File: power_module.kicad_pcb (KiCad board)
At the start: 4 copper layers, 95 x 110 mm, 71 parts, among them J1 USB_C_PD, J2 OUTPUT, J3 I2C_BREAKOUT, Q1 DUAL_N_FET, Q2 DUAL_N_FET, Q3 DUAL_N_FET, Q4 DUAL_N_FET, SW1 ON_OFF, U1 BQ7692003, U2 CH224K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

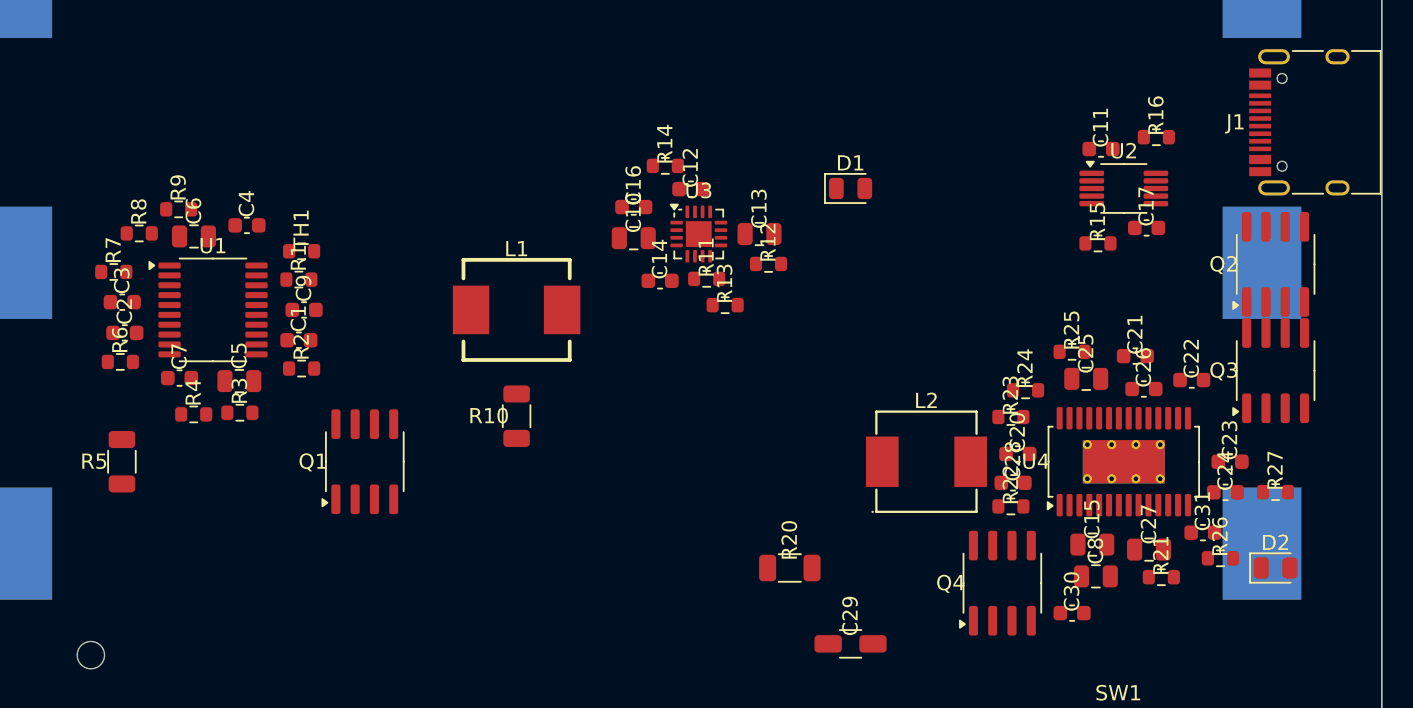
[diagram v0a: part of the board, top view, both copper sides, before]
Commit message: pcb: post-user spread pass — relieve crowding around U1 and U4
User adjustment pass moved BAT1 up and components into a compact
lower band; cluster-density check showed 17 components within 8mm
of U1 (BMS) and 17 within 8mm of U4 (buck-boost), too tight to route.

This pass:
  - Shifts U4 +6mm right (84,88) for thermal/edge clearance from
    BAT1 cell holder B.Cu pads (user-suggested in case the integrity-
    checker NPTH-via false positive was actually a ventilation concern).
  - Re-places 39 small parts via pin-targeted place_near against the
    correct U1 / U3 / U4 pad numbers, honoring the C9 → U1.9 explicit
    Placement_Anchor (the one the user noticed had missed last pass).
  - Fixes a Q2/Q3 mis-assumption: Q2 is actually the BQ24650 charger
    sync FET (BQ_HIDRV/BQ_LODRV/BQ_PH), not a buck-boost FET. Moved
    Q2 to the charger area near U3.14, Q3 stays near U4.28 as the
    BB_SW1-leg buck-boost FET.
  - Moves R27 out of U4's footprint into the D2 LED cluster.

0 integrity findings (no pad overlaps, no courtyard overlaps).
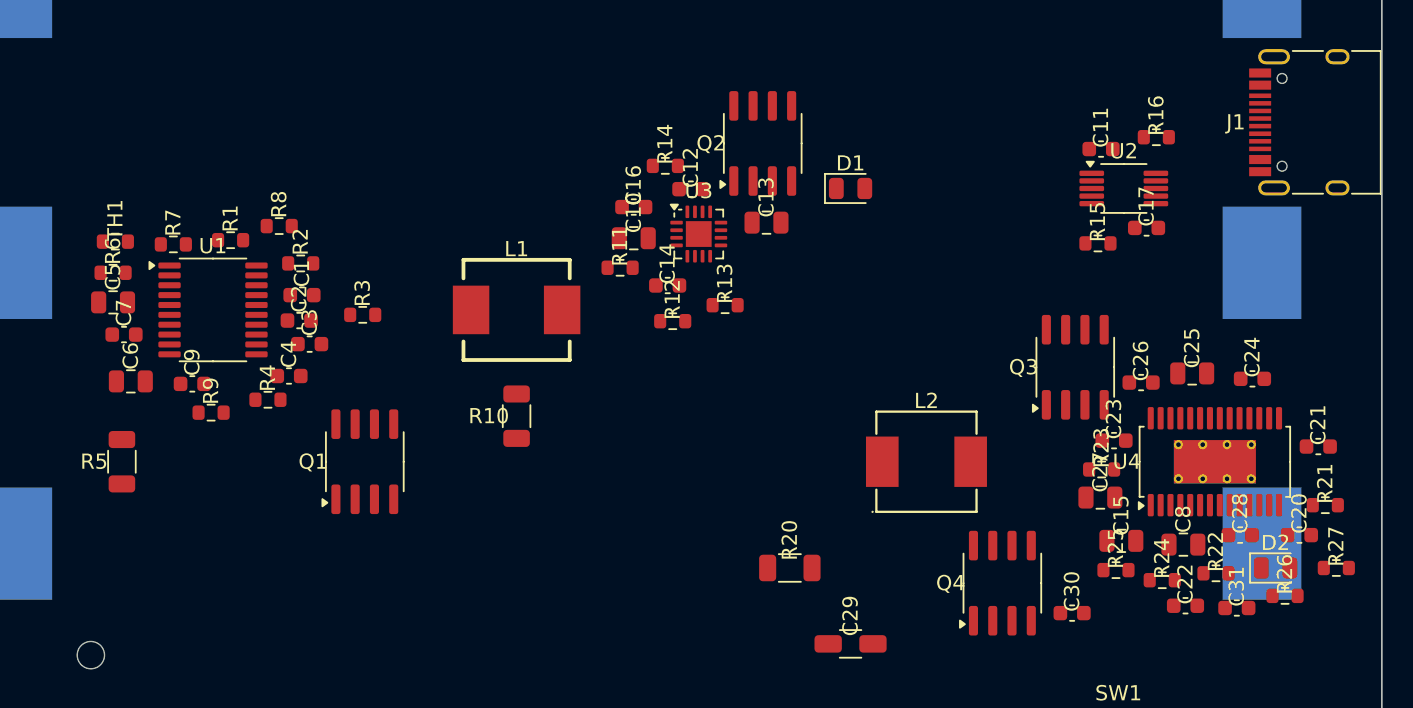
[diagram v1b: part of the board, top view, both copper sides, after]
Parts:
- moved Q2 34.7 mm to (54.2, 67.0)
- moved C20 19.3 mm to (89.6, 92.8)
- moved R24 15.4 mm to (80.5, 95.8)
- moved C28 15.4 mm to (85.7, 92.8)
- moved C22 14.9 mm to (82.1, 97.5)
- moved R25 14.7 mm to (77.5, 95.1)
- moved R22 14.2 mm to (84.1, 95.4)
- moved R9 13.6 mm to (17.9, 84.8)
- moved C21 13.4 mm to (90.8, 87.0)
- moved Q3 13.2 mm to (74.8, 81.8)
- moved C3 12.7 mm to (24.4, 80.3)
- moved TH1 12.3 mm to (11.6, 73.5)
- moved R21 11.8 mm to (91.3, 90.9)
- moved C2 11.5 mm to (23.7, 78.7)
- moved C6 10.4 mm to (12.6, 82.7)
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
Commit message: More minor shifting
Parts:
- moved SW1 33.2 mm to (91.5, 76.3), turned to 90 degrees
- moved C21 10.4 mm to (92.1, 97.3)
- moved R21 8.85 mm to (88.8, 99.4)
- moved U4 4.33 mm to (88.3, 87.8)
- moved C25 4.07 mm to (86.5, 81.7)
- moved C24 3.51 mm to (89.9, 81.8)
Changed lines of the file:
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@@
 	(footprint "Button_Switch_SMD:SW_SPDT_PCM12"
 		(layer "F.Cu")
-		(at 77.652724 106.455135)
+		(at 91.459276 76.250559 90)
 		(descr "Ultraminiature Surface Mount Slide Switch, right-angle, https://www.ckswitches.com/media/1424/pcm.pdf")
 		(property "Reference" "SW1"
-			(at 0 -3.2 0)
+			(at 0 -3.2 90)
 			(layer "F.SilkS")
 			(effects
@@
 		)
 		(property "Value" "ON_OFF"
-			(at 0 4.25 0)
+			(at 0 4.25 90)
 			(layer "F.Fab")
 			(effects
@@
 		)
 		(property "Datasheet" ""
-			(at 0 0 0)
+			(at 0 0 90)
 			(unlocked yes)
 			(layer "F.Fab")
@@
 		)
 		(property "Description" ""
-			(at 0 0 0)
+			(at 0 0 90)
 			(unlocked yes)
 			(layer "F.Fab")
@@
 		(attr smd)
 		(fp_line
-			(start -3.45 -0.07)
-			(end -3.45 0.72)
+			(start 1.4 -1.12)
+			(end 1.6 -1.12)
 			(stroke
 				(width 0.12)
@@
 		)
 		(fp_line
-			(start -2.85 1.73)
-			(end 2.85 1.73)
+			(start -1.6 -1.12)
+			(end 0.1 -1.12)
 			(stroke
 				(width 0.12)
@@
 		)
 		(fp_line
-			(start -1.6 -1.12)
-			(end 0.1 -1.12)
+			(start -3.45 -0.07)
+			(end -3.45 0.719999)
 			(stroke
 				(width 0.12)
@@
 		)
 		(fp_line
-			(start -1.4 1.73)
-			(end -1.4 3.02)
+			(start 3.45 0.719999)
+			(end 3.45 -0.07)
 			(stroke
 				(width 0.12)
@@
 		)
 		(fp_line
-			(start -1.4 3.02)
-			(end -1.2 3.23)
+			(start -1.4 1.73)
+			(end -1.4 3.02)
 			(stroke
 				(width 0.12)
@@
 		)
 		(fp_line
-			(start -1.2 3.23)
-			(end -0.3 3.23)
+			(start -2.85 1.73)
+			(end 2.85 1.73)
 			(stroke
 				(width 0.12)
@@
 		(fp_line
 			(start -0.1 3.02)
-			(end -0.3 3.23)
+			(end -0.1 1.73)
 			(stroke
 				(width 0.12)
@@
 		(fp_line
 			(start -0.1 3.02)
-			(end -0.1 1.73)
+			(end -0.3 3.23)
 			(stroke
 				(width 0.12)
@@
 		)
 		(fp_line
-			(start 1.4 -1.12)
-			(end 1.6 -1.12)
+			(start -1.4 3.02)
+			(end -1.2 3.23)
 			(stroke
 				(width 0.12)
@@
 		)
 		(fp_line
-			(start 3.45 0.72)
-			(end 3.45 -0.07)
+			(start -1.2 3.23)
+			(end -0.3 3.23)
 			(stroke
 				(width 0.12)
@@
 		)
 		(fp_line
-			(start -4.4 -2.45)
-			(end 4.4 -2.45)
+			(start 4.4 -2.45)
+			(end 4.4 2.1)
 			(stroke
 				(width 0.05)
@@
 		)
 		(fp_line
-			(start -4.4 2.1)
-			(end -4.4 -2.45)
+			(start -4.4 -2.45)
+			(end 4.4 -2.45)
 			(stroke
 				(width 0.05)
@@
 		)
 		(fp_line
-			(start -1.65 2.1)
-			(end -4.4 2.1)
+			(start 4.4 2.1)
+			(end 1.65 2.1)
 			(stroke
 				(width 0.05)
@@
 		)
 		(fp_line
-			(start -1.65 3.4)
-			(end -1.65 2.1)
+			(start 1.65 2.1)
+			(end 1.65 3.4)
 			(stroke
 				(width 0.05)
@@
 		)
 		(fp_line
-			(start 1.65 2.1)
-			(end 1.65 3.4)
+			(start -1.65 2.1)
+			(end -4.4 2.1)
 			(stroke
 				(width 0.05)
@@
 		)
 		(fp_line
-			(start 1.65 3.4)
-			(end -1.65 3.4)
+			(start -4.4 2.1)
+			(end -4.4 -2.45)
 			(stroke
 				(width 0.05)
@@
 		)
 		(fp_line
-			(start 4.4 -2.45)
-			(end 4.4 2.1)
+			(start 1.65 3.4)
+			(end -1.65 3.4)
 			(stroke
 				(width 0.05)
@@
 		)
 		(fp_line
-			(start 4.4 2.1)
-			(end 1.65 2.1)
+			(start -1.65 3.4)
+			(end -1.65 2.1)
 			(stroke
 				(width 0.05)
@@
 		)
 		(fp_line
-			(start -3.35 -1)
-			(end -3.35 1.6)
+			(start 3.35 -1)
+			(end -3.35 -1)
 			(stroke
 				(width 0.1)
@@
 		)
 		(fp_line
-			(start -3.35 1.6)
-			(end 3.35 1.6)
+			(start -3.35 -1)
+			(end -3.35 1.6)
 			(stroke
 				(width 0.1)
@@
 		)
 		(fp_line
-			(start -1.4 1.65)
-			(end -1.4 2.95)
+			(start 3.35 1.6)
+			(end 3.35 -1)
 			(stroke
 				(width 0.1)
@@
 		)
 		(fp_line
-			(start -1.4 2.95)
-			(end -1.2 3.15)
+			(start -3.35 1.6)
+			(end 3.35 1.6)
 			(stroke
 				(width 0.1)
@@
 		)
 		(fp_line
-			(start -1.2 3.15)
-			(end -0.35 3.15)
+			(start -1.4 1.65)
+			(end -1.399999 2.95)
 			(stroke
 				(width 0.1)
@@
 		)
 		(fp_line
-			(start -0.35 3.15)
-			(end -0.15 2.95)
+			(start -0.1 2.9)
+			(end -0.1 1.6)
 			(stroke
 				(width 0.1)
@@
 		)
 		(fp_line
-			(start -0.1 2.9)
-			(end -0.1 1.6)
+			(start -1.399999 2.95)
+			(end -1.2 3.149999)
 			(stroke
 				(width 0.1)
@@
 		)
 		(fp_line
-			(start 3.35 -1)
-			(end -3.35 -1)
+			(start -1.2 3.149999)
+			(end -0.35 3.15)
 			(stroke
 				(width 0.1)
@@
 		)
 		(fp_line
-			(start 3.35 1.6)
-			(end 3.35 -1)
+			(start -0.35 3.15)
+			(end -0.15 2.95)
 			(stroke
 				(width 0.1)
@@
 		)
 		(fp_text user "${REFERENCE}"
-			(at 0 -3.2 0)
+			(at 0 -3.2 90)
 			(layer "F.Fab")
 			(effects
@@
 		)
 		(pad "" smd rect
-			(at -3.65 -0.78)
+			(at -3.65 -0.78 90)
 			(size 1 0.8)
 			(layers "F.Cu" "F.Mask" "F.Paste")
 		)
 		(pad "" smd rect
-			(at -3.65 1.43)
+			(at -3.65 1.43 90)
 			(size 1 0.8)
 			(layers "F.Cu" "F.Mask" "F.Paste")
 		)
 		(pad "" np_thru_hole circle
-			(at -1.5 0.33)
+			(at -1.5 0.33 90)
 			(size 0.9 0.9)
 			(drill 0.9)
@@
 		)
 		(pad "" np_thru_hole circle
-			(at 1.5 0.33)
+			(at 1.5 0.33 90)
 			(size 0.9 0.9)
 			(drill 0.9)
@@
 		)
 		(pad "" smd rect
-			(at 3.65 -0.78)
+			(at 3.65 -0.78 90)
 			(size 1 0.8)
 			(layers "F.Cu" "F.Mask" "F.Paste")
 		)
 		(pad "" smd rect
-			(at 3.65 1.43)
+			(at 3.65 1.43 90)
 			(size 1 0.8)
 			(layers "F.Cu" "F.Mask" "F.Paste")
 		)
 		(pad "1" smd rect
-			(at -2.25 -1.43)
+			(at -2.25 -1.43 90)
 			(size 0.7 1.5)
 			(layers "F.Cu" "F.Mask" "F.Paste")
@@
 		)
 		(pad "2" smd rect
-			(at 0.75 -1.43)
+			(at 0.75 -1.43 90)
 			(size 0.7 1.5)
 			(layers "F.Cu" "F.Mask" "F.Paste")
@@
 		)
 		(pad "3" smd rect
-			(at 2.25 -1.43)
+			(at 2.25 -1.43 90)
 			(size 0.7 1.5)
 			(layers "F.Cu" "F.Mask" "F.Paste")
@@
 	(footprint "Capacitor_SMD:C_0805_2012Metric"
 		(layer "F.Cu")
-		(at 82.504056 82.183077)
+		(at 86.541974 81.671148)
 		(descr "Capacitor SMD 0805 (2012 Metric), square (rectangular) end terminal, IPC-7351 nominal, (Body size source: IPC-SM-782 page 76, https://www.pcb-3d.com/wordpress/wp-content/uploads/ipc-sm-782a_amendment_1_and_2.pdf, https://docs.google.com/spreadsheets/d/1BsfQQcO9C6DZCsRaXUlFlo91Tg2WpOkGARC1WS5S8t0/edit?usp=sharing), generated with kicad-footprint-generator")
 		(tags "capacitor")
@@
 	(footprint "Resistor_SMD:R_0603_1608Metric"
 		(layer "F.Cu")
-		(at 91.275 90.8625)
+		(at 88.827926 99.365086)
 		(descr "Resistor SMD 0603 (1608 Metric), square (rectangular) end terminal, IPC-7351 nominal, (Body size source: IPC-SM-782 page 72, https://www.pcb-3d.com/wordpress/wp-content/uploads/ipc-sm-782a_amendment_1_and_2.pdf), generated with kicad-footprint-generator")
 		(tags "resistor")
@@
 	(footprint "Capacitor_SMD:C_0603_1608Metric"
 		(layer "F.Cu")
-		(at 90.812984 87.000126)
+		(at 92.149844 97.316627)
 		(descr "Capacitor SMD 0603 (1608 Metric), square (rectangular) end terminal, IPC-7351 nominal, (Body size source: IPC-SM-782 page 76, https://www.pcb-3d.com/wordpress/wp-content/uploads/ipc-sm-782a_amendment_1_and_2.pdf), generated with kicad-footprint-generator")
 		(tags "capacitor")
@@
 	(footprint "Capacitor_SMD:C_0603_1608Metric"
 		(layer "F.Cu")
-		(at 86.474999 82.539424)
+		(at 89.896687 81.760211)
 		(descr "Capacitor SMD 0603 (1608 Metric), square (rectangular) end terminal, IPC-7351 nominal, (Body size source: IPC-SM-782 page 76, https://www.pcb-3d.com/wordpress/wp-content/uploads/ipc-sm-782a_amendment_1_and_2.pdf), generated with kicad-footprint-generator")
 		(tags "capacitor")
@@
 	(footprint "Package_SO:HTSSOP-28-1EP_4.4x9.7mm_P0.65mm_EP2.85x5.4mm_ThermalVias"
 		(layer "F.Cu")
-		(at 84 88 90)
+		(at 88.327946 87.754013 90)
 		(descr "HTSSOP, 28 Pin (https://pdfserv.maximintegrated.com/package_dwgs/21-0108.PDF), generated with kicad-footprint-generator ipc_gullwing_generator.py")
 		(tags "HTSSOP SO")

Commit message: Inspecting progress
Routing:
- net V12_OUT: track 0.00 -> 52.8 mm
- net GND: vias 0 -> 33
- net BAT+: vias 0 -> 10

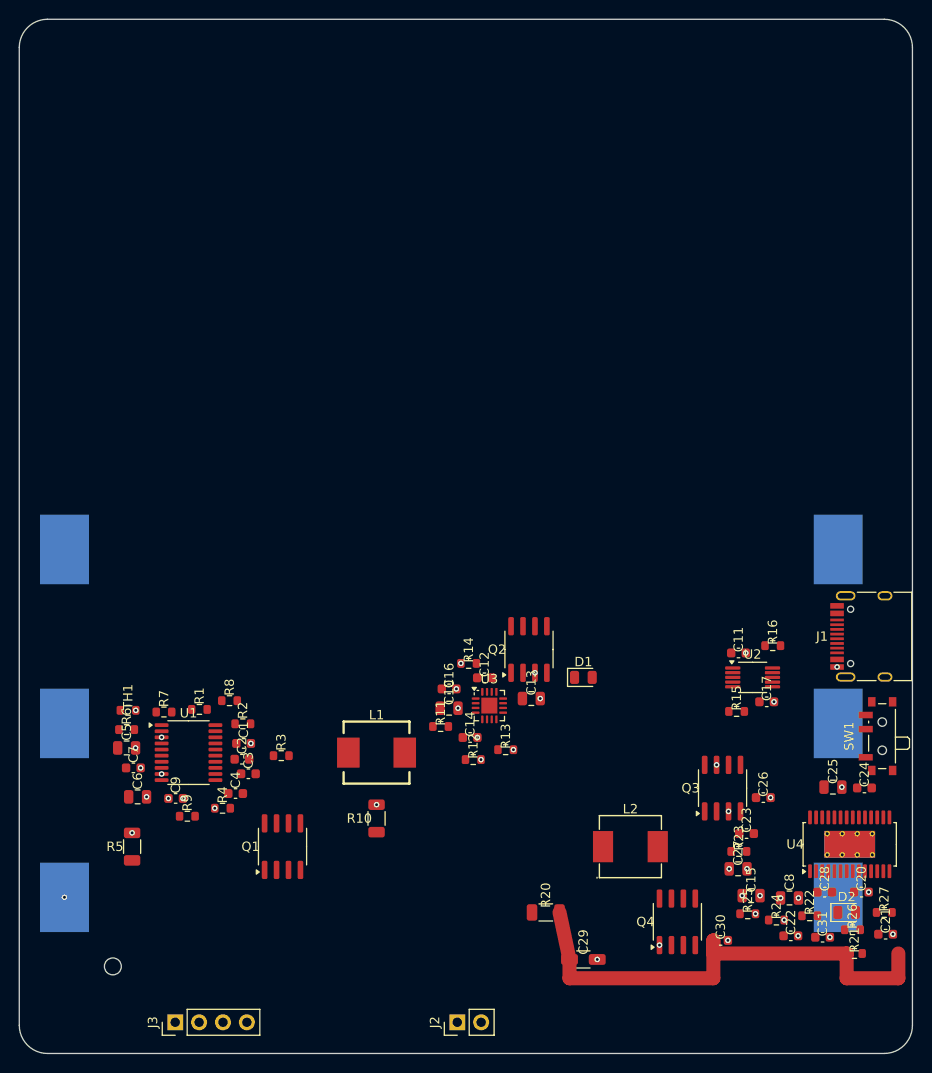
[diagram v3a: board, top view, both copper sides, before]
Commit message: pcb: north-spread BMS + charger into upper-half BAT1 envelope
Moved U1 BMS + Q1 + R5 sense + 17 satellites to NW quadrant (y=33-45),
moved U3 charger + L1 + R10 + Q2 + 9 satellites to NE quadrant
(y=35-45). Buck-boost U4 cluster stays south, output stage stays south.
The upper-half F.Cu was empty since BAT1 lives on B.Cu — used that
real estate to relieve density.

analyze_congestion result:
  - before: 5 cells score >= 238 (U1, U3, U4+BAT1, all ~270)
  - after: 2 cells score >= 238, both U4+BAT1 region (inherent
    buck-boost density). U1 and U3 hotspots dropped off the top-12.
  - active cells 85 -> 53, top score 272 -> 240.

Cell-sense routing also benefits: U1.VC pins are now at x=22-28 on
the left side of the board, ~17 mm from BAT1's left-side CELL pads
(x=4.8). Previously the path was ~85 mm round-trip.

0 errors / 1 warning (Q2/L1 minor courtyard overlap; nudged Q2).
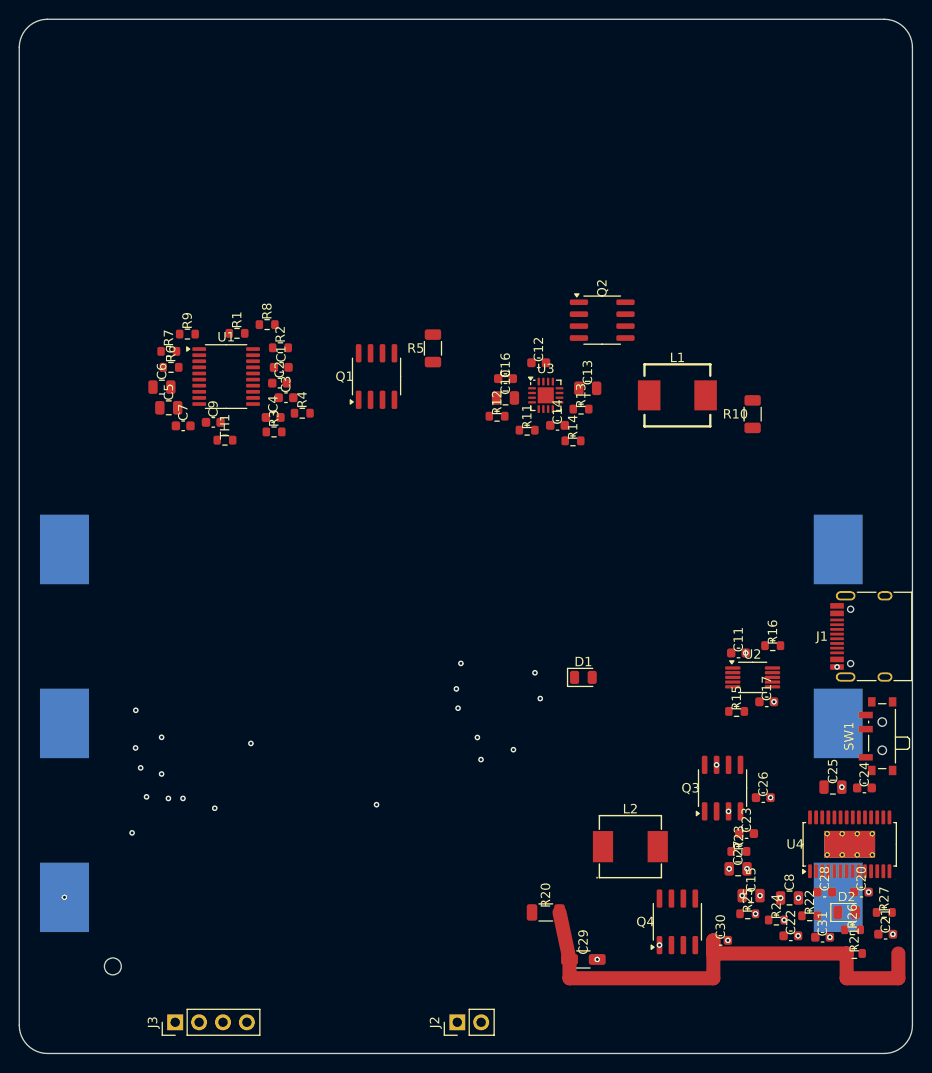
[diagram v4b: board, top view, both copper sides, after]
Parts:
- moved R5 61.9 mm to (44.0, 35.0)
- moved R10 58.7 mm to (78.0, 42.0)
- moved R9 51.3 mm to (17.9, 33.5)
- moved Q1 51.0 mm to (38.0, 38.0)
- moved L1 49.7 mm to (70.0, 40.0)
- moved C6 43.7 mm to (15.2, 39.1)
- moved R4 42.9 mm to (30.1, 41.9)
- moved C1 40.2 mm to (27.9, 37.0)
- moved C2 40.2 mm to (27.7, 38.7)
- moved C3 40.2 mm to (28.4, 40.3)
- moved C4 40.2 mm to (27.0, 42.4)
- moved C9 40.2 mm to (20.6, 42.9)
- moved R1 40.2 mm to (23.2, 33.4)
- moved R2 40.2 mm to (27.8, 34.9)
- moved R8 40.2 mm to (26.4, 32.5)
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
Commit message: Resized board and moved pieces back onto BAT1 area
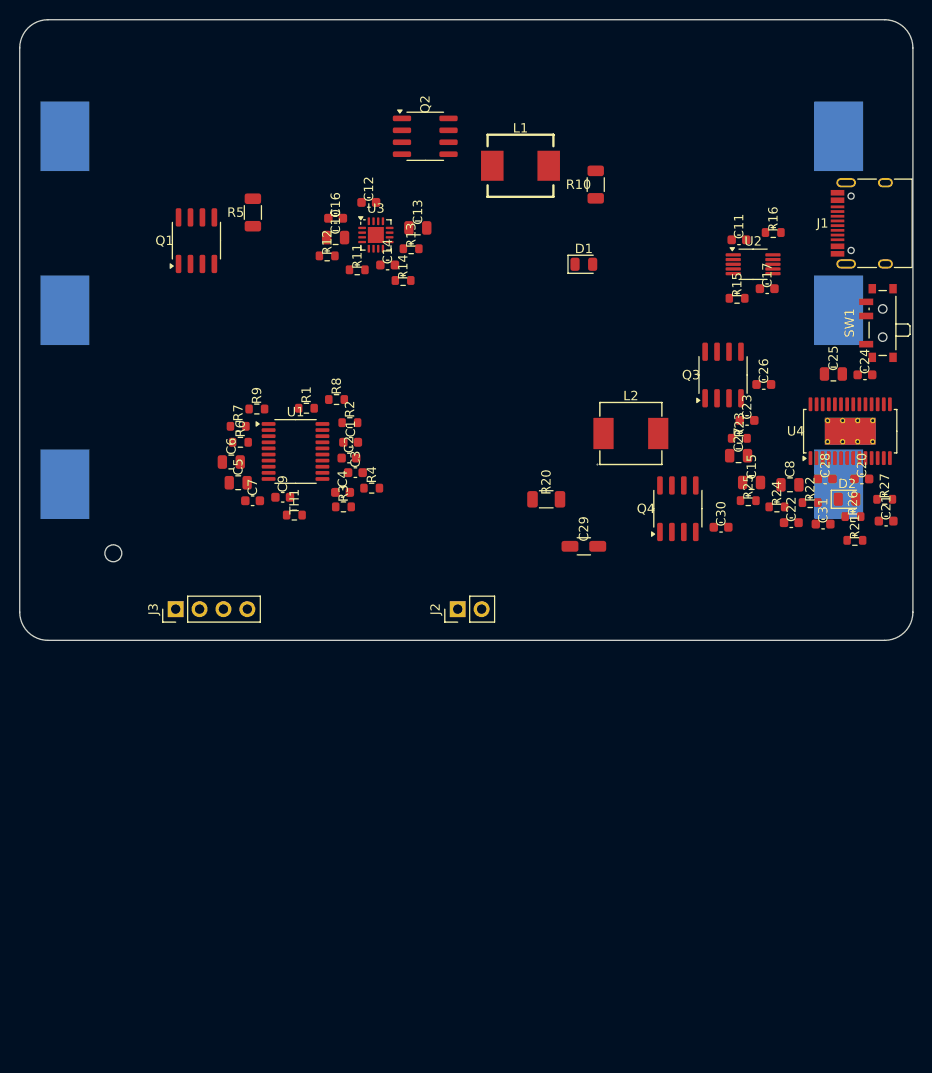
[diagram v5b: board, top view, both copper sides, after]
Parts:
- moved BAT1 43.9 mm to (46.0, 30.9)
- moved C17 43.9 mm to (79.5, 28.7)
- moved C23 43.9 mm to (77.4, 42.7)
- moved C26 43.9 mm to (79.2, 38.8)
- moved C27 43.9 mm to (76.5, 46.4)
- moved R15 43.9 mm to (76.3, 29.7)
- moved R21 43.9 mm to (88.9, 55.4)
- moved C21 43.9 mm to (92.2, 53.4)
- moved C22 43.9 mm to (82.1, 53.5)
- moved C24 43.9 mm to (89.9, 37.8)
- moved C25 43.9 mm to (86.6, 37.7)
- moved C29 43.9 mm to (60.0, 56.1)
- moved C30 43.9 mm to (74.6, 54.0)
- moved C31 43.9 mm to (85.5, 53.7)
- moved C8 43.9 mm to (82.0, 49.5)
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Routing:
- net V12_OUT: track 52.8 -> 0.00 mm
- net GND: vias 33 -> 0
- net BAT+: vias 10 -> 0
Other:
- board size 95 x 110 mm -> 95 x 66 mm
